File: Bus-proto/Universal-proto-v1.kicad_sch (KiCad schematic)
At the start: 51 parts, among them J1 Bus_ISA_8bit, J2 ISA Breakout, J3 Pico GPIO Breakout 2, J4 Pico GPIO Breakout 1, J5 Conn_01x20, J6 Conn_01x20, J7 Conn_01x20, J8 Conn_01x20, J9 Conn_02x02_Odd_Even

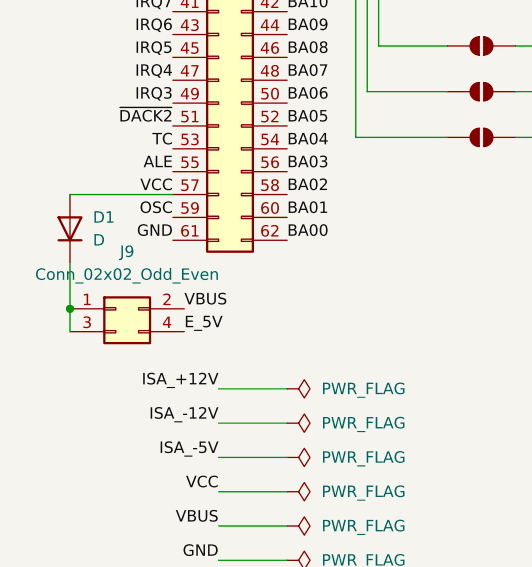
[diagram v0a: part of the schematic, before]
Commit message: Add MSX adapter
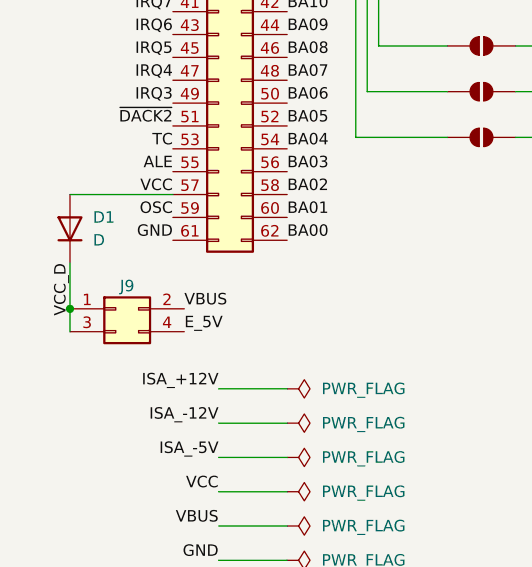
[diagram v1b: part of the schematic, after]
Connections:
- net VCC_D: now reaches D1.1 (K), J9.1 (Pin_1), J9.3 (Pin_3)
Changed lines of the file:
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@@
+		)
+	)
+	(label "VCC_D"
+		(at 20.32 109.22 270)
+		(effects
+			(font
+				(size 1.27 1.27)
+			)
+			(justify right bottom)
 		)
 	)
@@
 		(on_board yes)
 		(dnp no)
-		(fields_autoplaced yes)
 		(property "Reference" "J9"
-			(at 26.67 107.95 0)
+			(at 26.67 111.76 0)
 			(effects
 				(font
@@
 					(size 1.27 1.27)
 				)
-			)
-		)
+				(hide yes)
+			)
+		)
